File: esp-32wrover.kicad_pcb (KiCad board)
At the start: 2 copper layers, 68.6 x 53.3 mm, 92 parts, among them CON1 BARREL_JACK, P1 Power, P10 ICSP, P11 ICSP-1, P2 Analog, P3 Digital, P4 Digital, P5 CONN_1, P6 CONN_1, P7 CONN_1, P8 CONN_1, P9 CONN_01X04, Q1 12Mhz, Q2 32.768Khz, Q3 Q_NPN_BEC, Q4 Q_NPN_BEC, SW1 SW_PUSH, SW2 SW_PUSH, U1 usb_mini_b, U2 MCP16311-MNY, U3 BD00GA5WEFJ, U4 PL2303HXA, U5 MCP6001R, U6 ESP32-WROVER, U7 IRLM6402

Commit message: sap xep linh kien
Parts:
- removed Q1: 12Mhz, Crystals:Q_49U3HMS
- removed Q2: 32.768Khz, Crystals:Crystal_SMD_Micro-Crystal_MS1V-T1K
- removed R23, R25, R27, R29, R31, R33: 220k/1%, Resistors_SMD:R_0603
- removed R24, R26, R28, R30, R32, R34: 100k, Resistors_SMD:R_0603
- added Y1: 12Mhz, Crystals:Q_49U3HMS, F.Cu at (135.9, 87.6)
- added Y2: 32.768Khz, Crystals:Crystal_SMD_Micro-Crystal_MS1V-T1K, F.Cu at (155.1, 88.6)
- D1, D3: value D_Schottky_Small -> SS24
- P11: footprint Pin_Headers:Pin_Header_Angled_2x03_Pitch2.54mm -> Pin_Headers:Pin_Header_Straight_2x03_Pitch2.54mm
- moved R1 116.6 mm to (125.3, 80.1), turned to 90 degrees
- moved R5 116.6 mm to (127.4, 93.9), turned to 180 degrees
- moved SW2 113.5 mm to (117.3, 79.6)
- moved R16 113.4 mm to (122.6, 94.9), turned to 180 degrees
- moved R2 109.4 mm to (123.7, 83.4), turned to 90 degrees
- moved SW1 105.2 mm to (117.3, 75.3)
- moved R21 105.1 mm to (119.1, 96.6)
- moved R22 104.0 mm to (122.6, 96.8)
- moved P9 101.9 mm to (113.4, 96.9)
- moved D5 101.2 mm to (125.6, 90.7), turned to 180 degrees
- moved D6 99.5 mm to (174.0, 112.1), turned to 180 degrees
- moved R20 99.0 mm to (137.0, 102.4), turned to 90 degrees
- moved R15 98.1 mm to (122.6, 98.7), turned to 180 degrees
- moved R19 93.7 mm to (139.4, 102.4), turned to 270 degrees
- moved D7 93.3 mm to (174.1, 110.6), turned to 180 degrees
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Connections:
- CON1 pad 2: Net-(CON1-Pad2) -> GND
- D10 pad 2: A5 -> ADC-5
- D11 pad 2: A3 -> ADC-3
- D6 pad 2: Net-(D6-Pad2) -> ADC-0
- D7 pad 2: A1 -> ADC-1
- D8 pad 2: A2 -> ADC-2
- D9 pad 2: A4 -> ADC-4
- P1 pad 2: Net-(P1-Pad2) -> (no net)
- P11 pad 1: Net-(P11-Pad1) -> (no net)
- P11 pad 3: Net-(P11-Pad3) -> (no net)
- P11 pad 4: Net-(P11-Pad4) -> (no net)
- P11 pad 5: Net-(P11-Pad5) -> (no net)
- P4 pad 1: RXD -> GPIO0
- P4 pad 2: TXD -> GPIO2
- P4 pad 3: GPIO0 -> IO12
- P4 pad 4: GPIO2 -> IO13
- P4 pad 5: IO12 -> IO14
- P4 pad 6: IO13 -> IO15
- P4 pad 7: IO14 -> TXD
- P4 pad 8: IO15 -> RXD
- P5 pad 1: Net-(P5-Pad1) -> (no net)
- P6 pad 1: Net-(P6-Pad1) -> (no net)
- P7 pad 1: Net-(P7-Pad1) -> (no net)
- P8 pad 1: Net-(P8-Pad1) -> (no net)
- U1 pad 4: Net-(U1-Pad4) -> (no net)
- U3 pad 4: Net-(U3-Pad4) -> (no net)
- U3 pad 6: Net-(U3-Pad6) -> (no net)
- U3 pad 7: Net-(U3-Pad7) -> (no net)
- U4 pad 11: Net-(U4-Pad11) -> (no net)
- U4 pad 12: Net-(U4-Pad12) -> (no net)
- U4 pad 13: Net-(U4-Pad13) -> (no net)
- U4 pad 14: Net-(U4-Pad14) -> (no net)
- U4 pad 19: Net-(U4-Pad19) -> (no net)
- U4 pad 22: Net-(U4-Pad22) -> (no net)
- U4 pad 23: Net-(U4-Pad23) -> (no net)
- U4 pad 24: Net-(U4-Pad24) -> (no net)
- U4 pad 6: Net-(U4-Pad6) -> (no net)
- U4 pad 8: Net-(U4-Pad8) -> (no net)
- U4 pad 9: Net-(U4-Pad9) -> (no net)
- U6 pad 10: A4 -> ADC-4
- U6 pad 11: A5 -> ADC-5
- U6 pad 32: Net-(U6-Pad32) -> (no net)
- U6 pad 39: Net-(U6-Pad39) -> (no net)
- U6 pad 5: A1 -> ADC-1
- U6 pad 6: A2 -> ADC-2
- U6 pad 7: A3 -> ADC-3

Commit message: đi dây PCB
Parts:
- removed P11: ICSP-1, Pin_Headers:Pin_Header_Straight_2x03_Pitch2.54mm
- moved C16 12.2 mm to (139.4, 114.3), turned to 0 degrees
- moved D10 9.79 mm to (174.3, 114.3)
- moved D6 6.49 mm to (174.4, 105.6)
- moved D9 6.23 mm to (174.3, 112.3)
- moved C17 5.88 mm to (143.1, 116.4), turned to 0 degrees
- moved P10 5.57 mm to (176.9, 100.9), turned to 180 degrees
- moved R10 4.66 mm to (131.6, 112.2), turned to 0 degrees
- moved R17 4.66 mm to (127.4, 110.0)
- moved R3 4.21 mm to (127.8, 93.5)
- moved C6 3.69 mm to (127.6, 112.0), turned to 0 degrees
- moved R9 3.51 mm to (124.7, 113.9)
- moved D7 3.44 mm to (174.4, 107.2)
- moved D11 3.20 mm to (174.4, 110.7)
- moved D3 2.81 mm to (114.7, 105.3), turned to 90 degrees
- moved C7 2.62 mm to (139.9, 82.9)
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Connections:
- P1 pad 1: IO18 -> (no net)
- P3 pad 1: CMD -> SD1
- P3 pad 10: IO27 -> IO14
- P3 pad 2: CLK -> SDO
- P3 pad 3: SDO -> CLK
- P3 pad 5: SD1 -> CMD
- P3 pad 6: SD2 -> SD3
- P3 pad 7: SD3 -> SD2
- P3 pad 8: IO17 -> IO13
- P3 pad 9: IO16 -> IO12
- P4 pad 1: GPIO0 -> IO27
- P4 pad 2: GPIO2 -> IO15
- P4 pad 3: IO12 -> GPIO2
- P4 pad 4: IO13 -> GPIO0
- P4 pad 5: IO14 -> IO16
- P4 pad 6: IO15 -> IO17
- U6 pad 30: IO18 -> (no net)
- U6 pad 31: IO27 -> (no net)
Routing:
- net GND: track 0.00 -> 406.1 mm, vias 0 -> 11
- net +3V3: track 0.00 -> 175.5 mm, vias 0 -> 3
- net EN: track 0.00 -> 136.3 mm, vias 0 -> 4
- net RXD: track 0.00 -> 109.7 mm, vias 0 -> 3
- net TXD: track 0.00 -> 107.4 mm, vias 0 -> 1
- net GPIO0: track 0.00 -> 106.6 mm, vias 0 -> 3
- net +5V: track 0.00 -> 79.6 mm, vias 0 -> 1
- net VCC: track 0.00 -> 74.2 mm, vias 0 -> 3
- net Vin: track 0.00 -> 57.5 mm, vias 0 -> 2
- net SDA: track 0.00 -> 54.3 mm, vias 0 -> 1
- net GPIO2: track 0.00 -> 53.9 mm, vias 0 -> 1
- net SCL: track 0.00 -> 52.2 mm, vias 0 -> 1
- net IO17: track 0.00 -> 49.7 mm, vias 0 -> 1
- net IO16: track 0.00 -> 49.0 mm, vias 0 -> 1
- net Net-(R13-Pad1): track 0.00 -> 48.7 mm, vias 0 -> 2
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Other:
- net class Default: via_dia 0.6 -> 1; via_drill 0.4 -> 0.6

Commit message: xoá file autosave
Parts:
- moved R9 14.6 mm to (119.1, 100.3), turned to 0 degrees
- moved C9 0.49 mm to (120.1, 111.7)
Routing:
- net GND: track 406.1 -> 390.4 mm
- net Net-(R10-Pad1): track 14.8 -> 30.1 mm, vias 0 -> 2
- net +5V: track 79.6 -> 74.5 mm
- net VCC: track 74.2 -> 78.8 mm
- net Net-(D2-Pad2): track 16.0 -> 19.4 mm
- net SDO: track 39.8 -> 42.2 mm
- net Net-(R4-Pad1): track 23.4 -> 25.6 mm
- net SD1: track 42.5 -> 44.6 mm
- net SDA: track 54.3 -> 56.1 mm
- net CLK: track 37.0 -> 38.5 mm
- net Net-(C6-Pad1): track 6.01 -> 7.34 mm
- net +3V3: track 175.5 -> 176.6 mm
- net Net-(R13-Pad1): track 48.7 -> 49.5 mm
- net Net-(R3-Pad1): track 13.8 -> 14.6 mm
- net SD2: track 28.7 -> 28.0 mm
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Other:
- net class Default: via_drill 0.6 -> 0.5

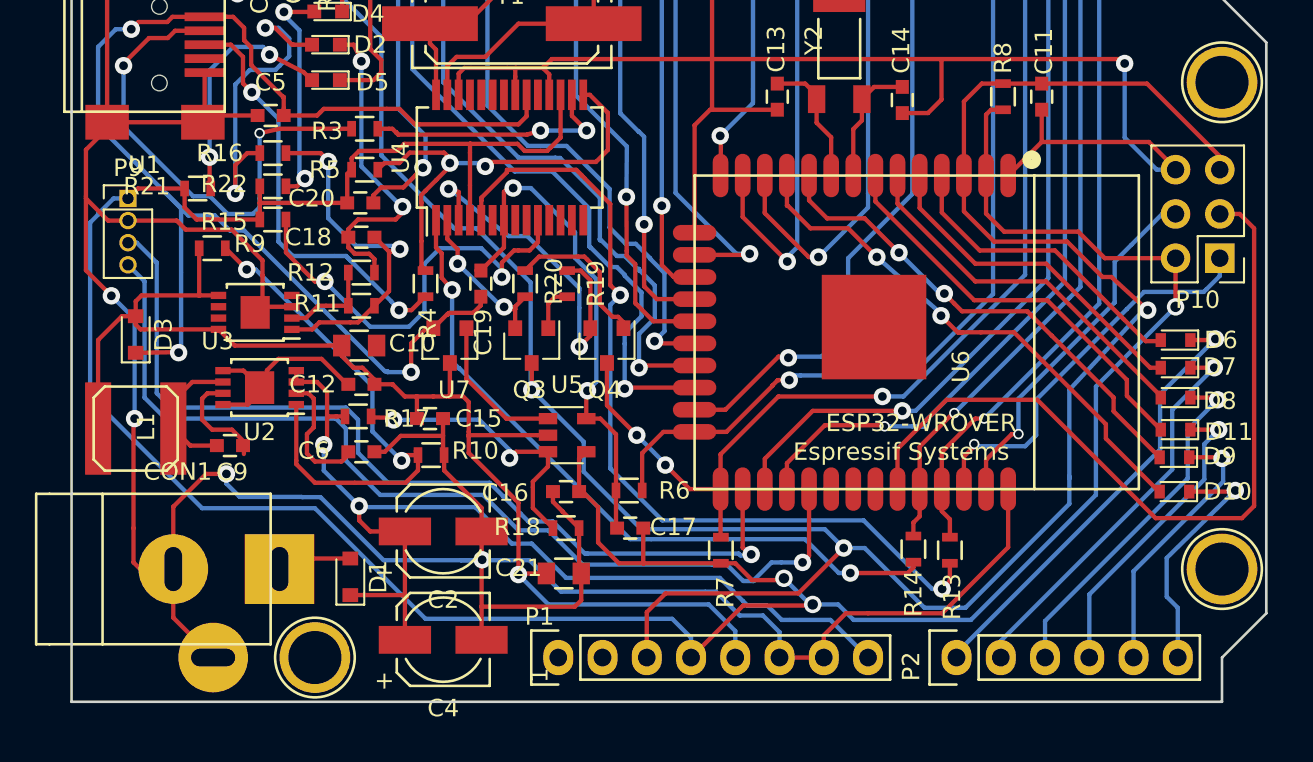
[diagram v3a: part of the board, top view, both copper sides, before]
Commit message: điều chỉnh độ rộng đường đi dây theo đúng quy cách
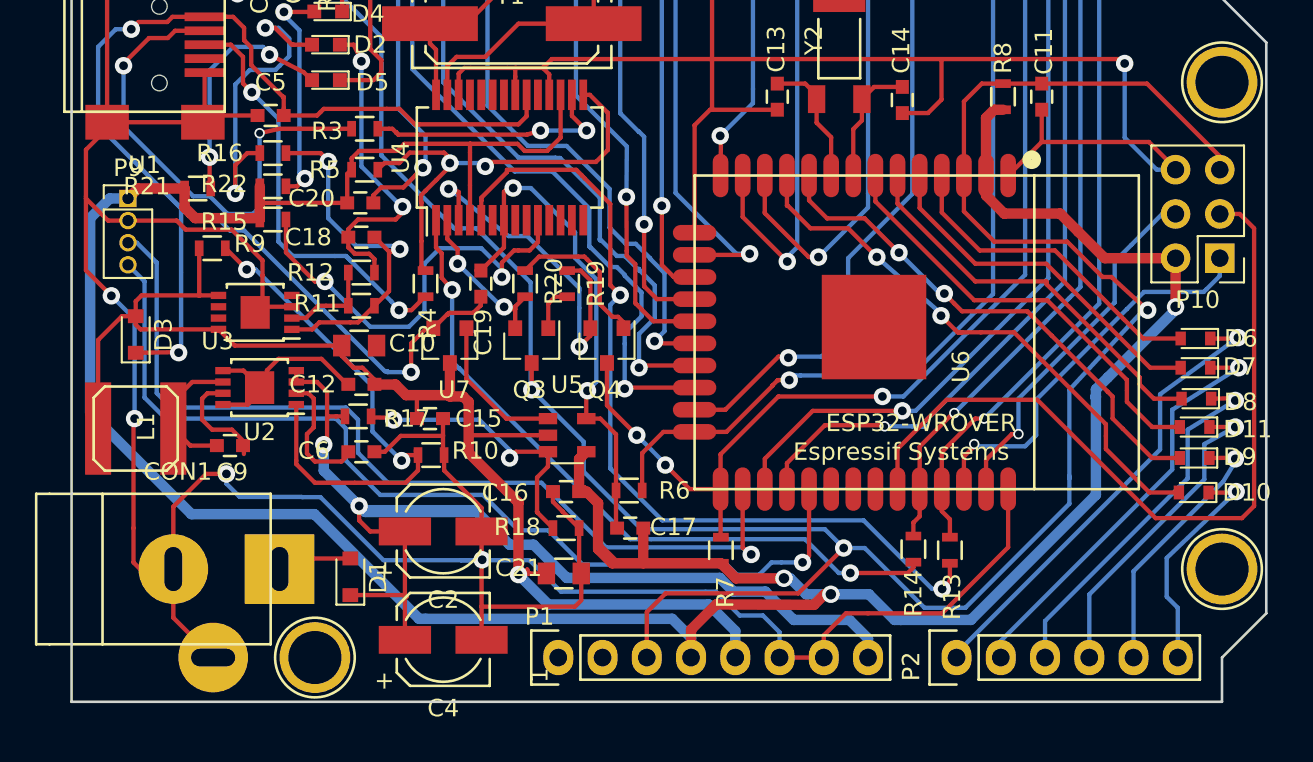
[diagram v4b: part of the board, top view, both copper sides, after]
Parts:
- moved D8 1.20 mm to (175.6, 109.0)
- moved D9 1.16 mm to (175.5, 112.4)
- moved D6 1.15 mm to (175.5, 105.5)
- moved D7 1.14 mm to (175.5, 107.2)
- moved D10 1.11 mm to (175.4, 114.4)
- moved D11 1.10 mm to (175.5, 110.6)
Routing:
- net Vin: track 57.4 -> 83.4 mm
- net +3V3: track 176.6 -> 199.9 mm
- net +5V: track 74.5 -> 83.7 mm
- net ADC-2: track 21.4 -> 23.0 mm
- net ADC-5: track 30.6 -> 32.1 mm
- net ADC-4: track 28.1 -> 29.6 mm
- net A1: track 23.1 -> 24.5 mm
- net ADC-3: track 23.8 -> 25.1 mm
- net A0: track 25.9 -> 27.1 mm
- net ADC-0: track 17.8 -> 18.9 mm
- net ADC-1: track 19.5 -> 20.6 mm
- net A5: track 14.4 -> 13.4 mm
- net A3: track 17.8 -> 18.5 mm
- net A2: track 20.5 -> 21.1 mm
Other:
- net class Default: trace_width 0.25 -> 0.6
- net class add added: clearance 0.2, trace_width 0.6, via_dia 1, via_drill 0.5

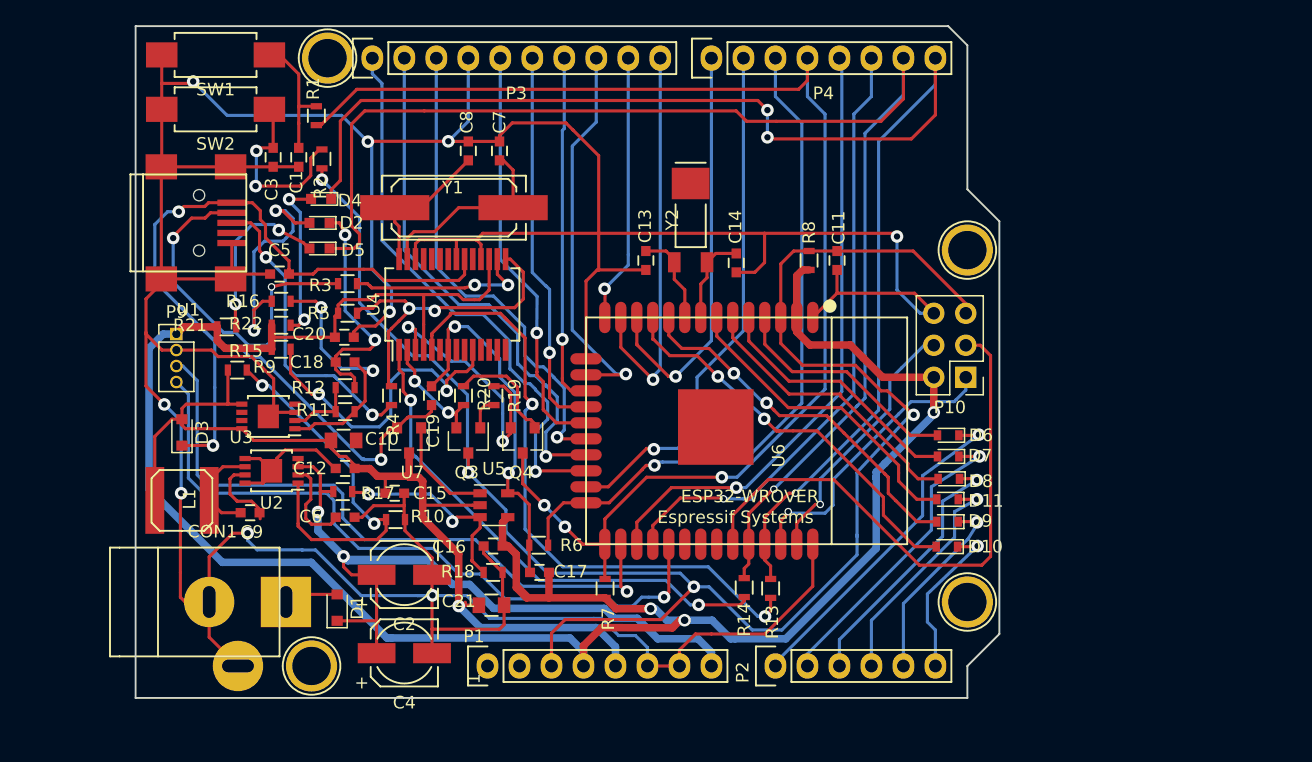
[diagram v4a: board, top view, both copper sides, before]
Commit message: sửa thư viện chân cho esp32-wrover
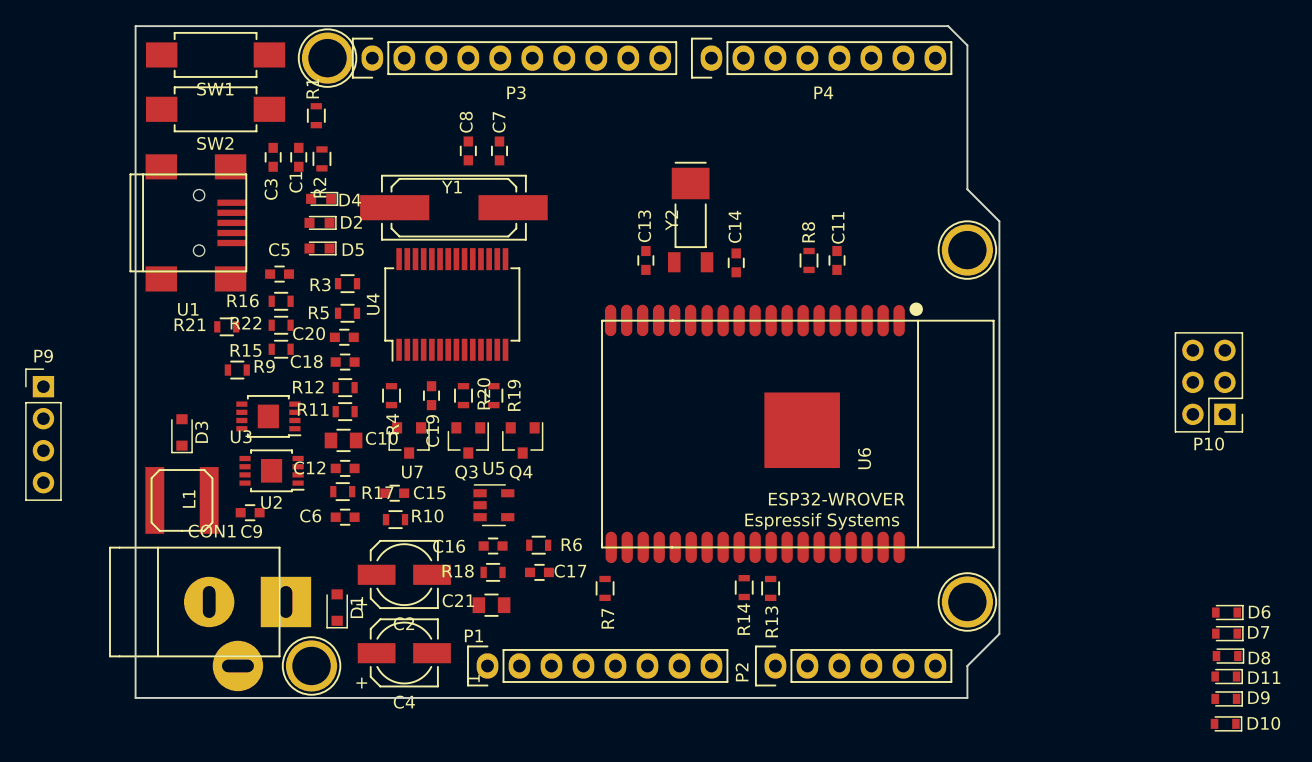
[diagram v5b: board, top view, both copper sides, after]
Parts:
- P9: footprint Pin_Headers:Pin_Header_Straight_1x04_Pitch1.27mm -> Pin_Headers:Pin_Header_Straight_1x04_Pitch2.54mm
- U6: footprint ESP32-footprints-Lib:ESP32-WROOM -> thu-vien:esp32-wrover
- moved D10 26.2 mm to (197.5, 128.4)
- moved D11 26.2 mm to (197.6, 124.7)
- moved D8 26.2 mm to (197.7, 123.0)
- moved D9 26.2 mm to (197.6, 126.4)
- moved D6 26.2 mm to (197.6, 119.6)
- moved D7 26.2 mm to (197.6, 121.3)
- moved P10 20.8 mm to (197.5, 103.8)
- moved P9 11.4 mm to (103.7, 101.7)
- moved U6 6.86 mm to (166.4, 105.4)
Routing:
- net GND: track 390.4 -> 0.00 mm, vias 11 -> 0
- net +3V3: track 199.9 -> 0.00 mm, vias 3 -> 0
- net EN: track 136.2 -> 0.00 mm, vias 4 -> 0
- net RXD: track 109.7 -> 0.00 mm, vias 3 -> 0
- net TXD: track 107.4 -> 0.00 mm, vias 1 -> 0
- net GPIO0: track 106.6 -> 0.00 mm, vias 3 -> 0
- net +5V: track 83.7 -> 0.00 mm, vias 1 -> 0
- net Vin: track 83.4 -> 0.00 mm, vias 2 -> 0
- net VCC: track 78.8 -> 0.00 mm, vias 3 -> 0
- net SDA: track 55.7 -> 0.00 mm, vias 1 -> 0
- net GPIO2: track 54.3 -> 0.00 mm, vias 1 -> 0
- net SCL: track 52.7 -> 0.00 mm, vias 1 -> 0
- net IO17: track 49.7 -> 0.00 mm, vias 1 -> 0
- net Net-(R13-Pad1): track 49.5 -> 0.00 mm, vias 2 -> 0
- net IO16: track 49.0 -> 0.00 mm, vias 1 -> 0
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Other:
- net class Default: trace_width 0.6 -> 0.25
